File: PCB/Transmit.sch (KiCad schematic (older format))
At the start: 8 parts

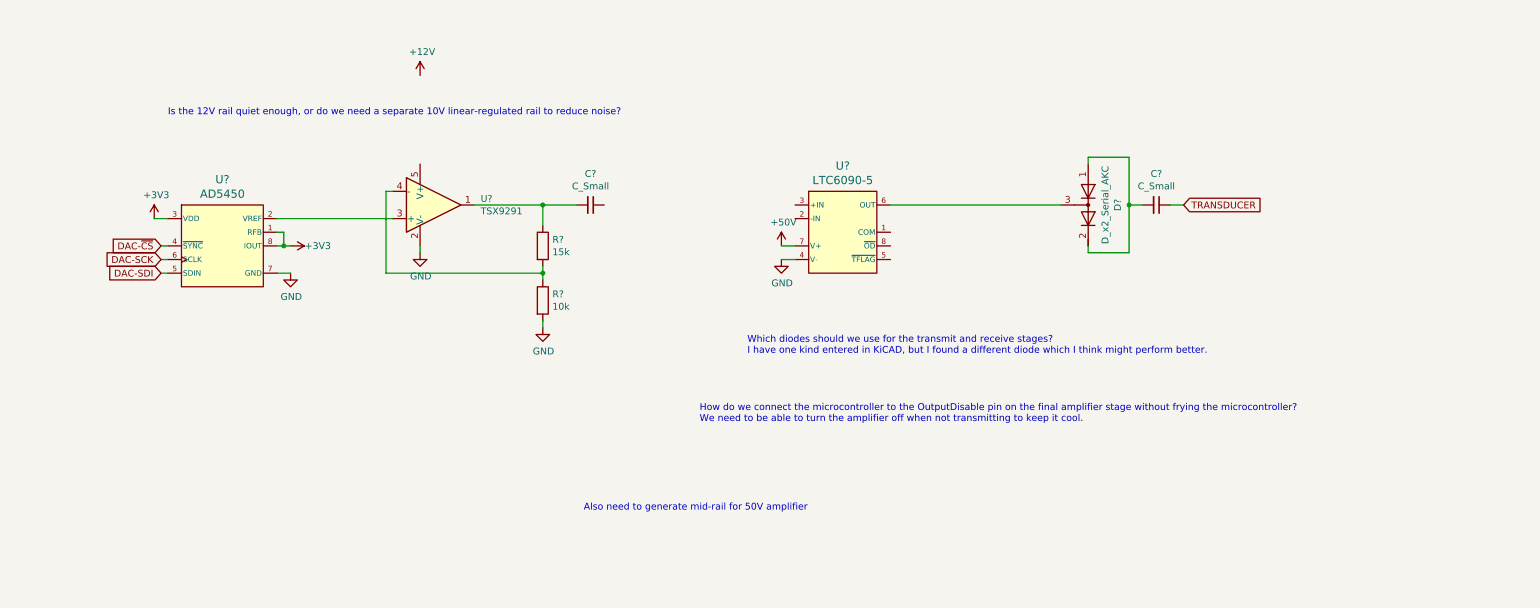
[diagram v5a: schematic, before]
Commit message: Switch to diodes that will waste less transmit power, add amplifier to generate transmit midrail, add enable signal to final amplifier
Enable signal to final amplifier is important, as it will allow us to conserve power when not transmitting. This should help keep the amplifier from overheating.
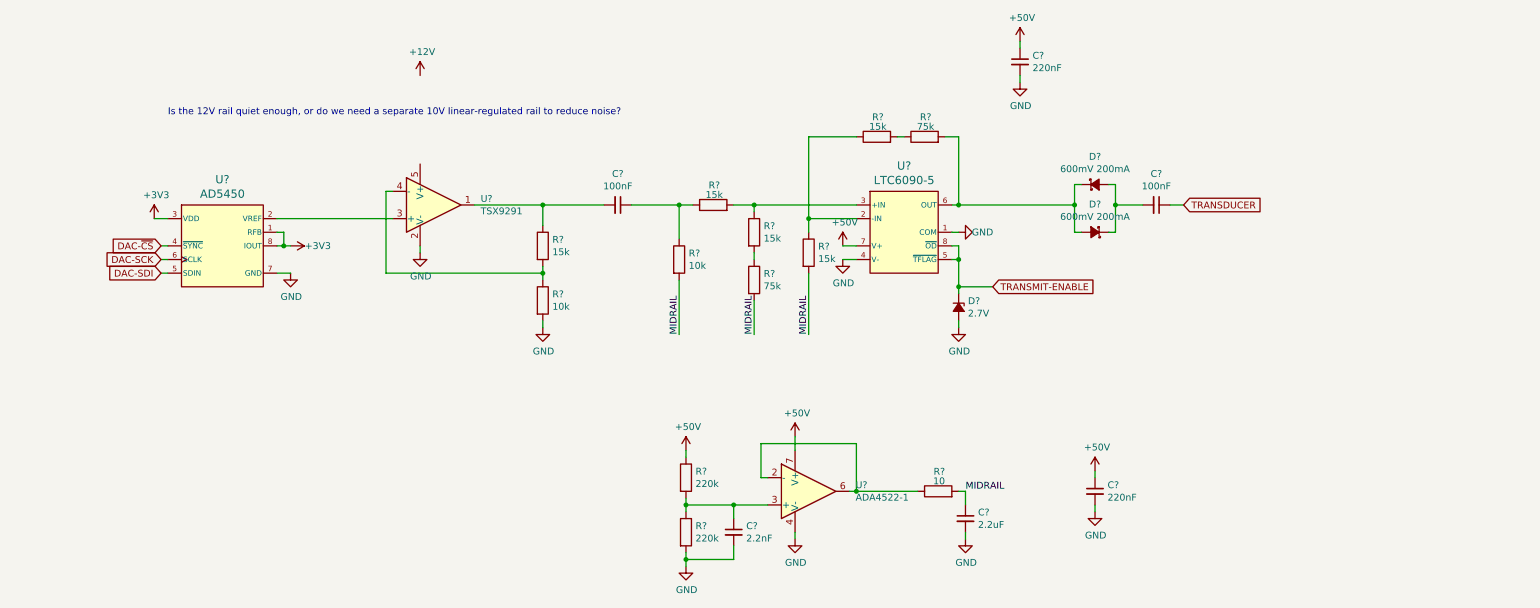
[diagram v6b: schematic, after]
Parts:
- removed C?: C_Small, symbol Device:C_Small
- removed D?: D_x2_Serial_AKC, Parts:MMBD7000L, symbol Device:D_x2_Serial_AKC
- added C?: 100nF, Capacitors_SMD:C_1206_HandSoldering, symbol Device:C_Small
- added C?: 2.2uF, Capacitors_SMD:C_1210_HandSoldering, symbol Device:C_Small
- added C? (x2): 220nF, Capacitors_SMD:C_1206_HandSoldering, symbol Device:C_Small
- added C?: 2.2nF, Capacitors_SMD:C_0603_HandSoldering, symbol Device:C_Small
- added D? (x2): 600mV 200mA, Diodes_SMD:D_SOD-523, symbol Device:D_Schottky_Small_ALT
- added D?: 2.7V, Diodes_SMD:D_SOD-123, symbol Device:D_Zener_Small_ALT
- added R? (x4): 15k, Resistors_SMD:R_0603_HandSoldering, symbol Device:R
- added R? (x2): 75k, Resistors_SMD:R_0603_HandSoldering, symbol Device:R
- added R?: 10, Resistors_SMD:R_0603_HandSoldering, symbol Device:R
- added R? (x2): 220k, Resistors_SMD:R_0603_HandSoldering, symbol Device:R
- added R?: 10k, Resistors_SMD:R_0603_HandSoldering, symbol Device:R
- added U?: ADA4522-1, Parts:SSOP8, symbol Parts:ADA4522-1
- C?: value C_Small -> 100nF; footprint (none) -> Capacitors_SMD:C_1206_HandSoldering
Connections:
- net +50V: now also C?.1, C?.1, R?.1, U?.7 (V+)
- net GND: now also U?.1 (COM), C?.2, C?.2, C?.2, C?.2, D?.2 (A), R?.2, U?.4 (V-)
- net TRANSDUCER: now also C?.1
- net at U?.6 (OUT): now also D?.1 (K), D?.2 (A), R?.2
- net at C?.1: now also R?.1, R?.1
- net at U?.2 (-IN): now also R?.1, R?.1
- net at U?.3 (+IN): now also R?.1, R?.2
- net TRANSMIT-ENABLE: now reaches U?.5 (~TFLAG)
- net TRANSMIT-ENABLE: now also U?.8 (~OD), D?.1 (K)
- new net: R?.1, R?.2 (x2)
- new net: C?.2, D?.1 (K), D?.2 (A)
- new net: R?.1, U?.2 (-), U?.6
- new net: C?.1, R?.1, R?.2, U?.3 (+)
- new net MIDRAIL: C?.1, R?.2, R?.2, R?.2, R?.2
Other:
- note removed: "Also need to generate mid-rail for 50V amplifier"
- note removed: "How do we connect the microcontroller to the OutputDisable pin on the final amplifier stage without frying the microcontroller?\nWe need to be able to turn the amplifier off when not transmitting to keep it cool."
- note removed: "Which diodes should we use for the transmit and receive stages?\nI have one kind entered in KiCAD, but I found a different diode which I think might perform better."
- moved on the sheet: C?, U?

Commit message: Add decoupling for other FPGA supplies
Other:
- note added: "Needs decoupling cap"
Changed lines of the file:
@@
 Wire Wire Line
 	8650 5800 8650 5850
+Text Notes 3250 3100 0    50   ~ 0
+Needs decoupling cap
 $EndSCHEMATC

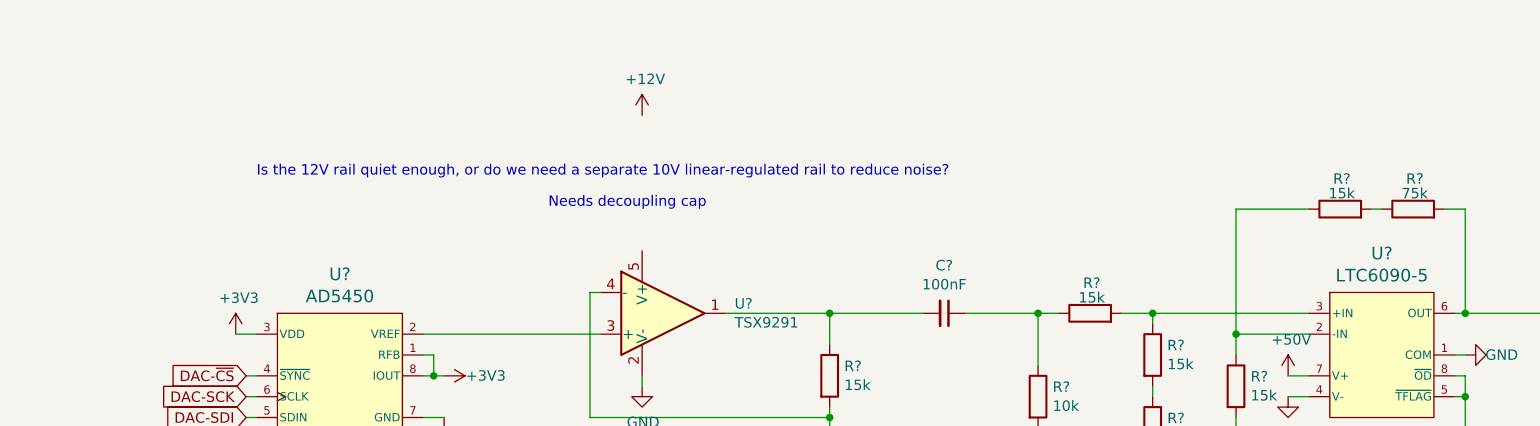
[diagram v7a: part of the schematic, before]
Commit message: Add decoupling capacitors for components without
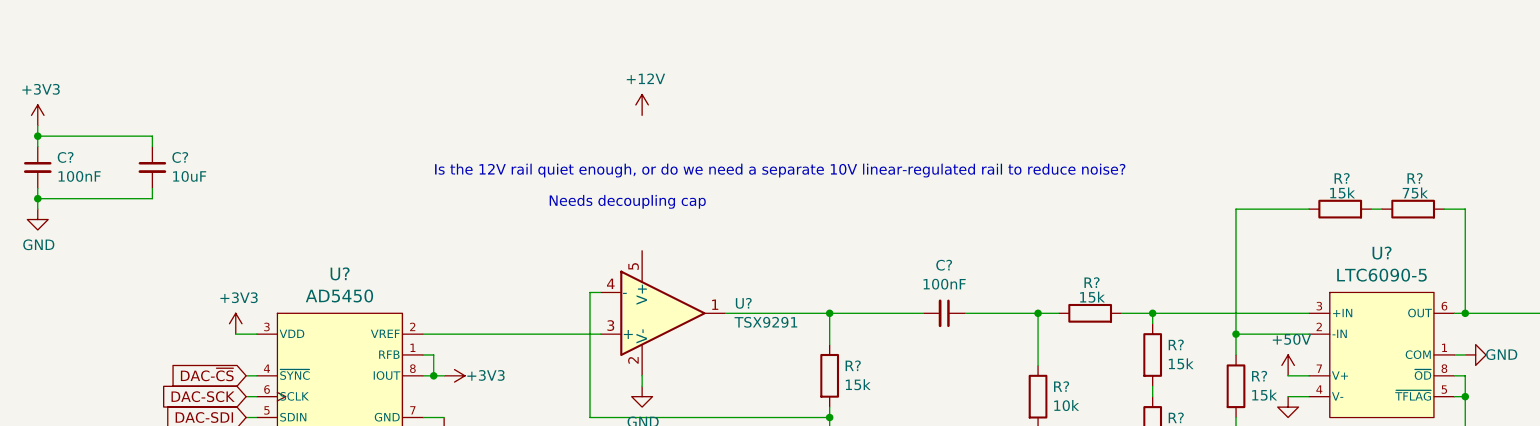
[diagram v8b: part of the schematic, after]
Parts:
- added C?: 100nF, Capacitors_SMD:C_0603_HandSoldering, symbol Device:C_Small
- added C?: 10uF, Capacitors_SMD:C_0805_HandSoldering, symbol Device:C_Small
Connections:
- net +3V3: now also C?.1, C?.1
- net GND: now also C?.2, C?.2
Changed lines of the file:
@@
 	1    0    0    -1
 $EndComp
-Text Notes 1850 2950 0    50   ~ 0
+Text Notes 2700 2950 0    50   ~ 0
 Is the 12V rail quiet enough, or do we need a separate 10V linear-regulated rail to reduce noise?
 $Comp
@@
 Text Notes 3250 3100 0    50   ~ 0
 Needs decoupling cap
+$Comp
+L power:GND #PWR?
+U 1 1 5E3B7B63
+P 800 3100
+F 0 "#PWR?" H 800 2850 50  0001 C CNN
+F 1 "GND" H 805 2927 50  0000 C CNN
+F 2 "" H 800 3100 50  0001 C CNN
+F 3 "" H 800 3100 50  0001 C CNN
+	1    800  3100
+	1    0    0    -1
+$EndComp
+$Comp
+L Device:C_Small C?
+U 1 1 5E3B80F6
+P 800 2900
+F 0 "C?" H 892 2946 50  0000 L CNN
+F 1 "100nF" H 892 2855 50  0000 L CNN
+F 2 "Capacitors_SMD:C_0603_HandSoldering" H 800 2900 50  0001 C CNN
+F 3 "https://www.digikey.ca/product-detail/en/w-rth-elektronik/885012206020/732-7939-1-ND/5454566" H 800 2900 50  0001 C CNN
+	1    800  2900
+	1    0    0    -1
+$EndComp
+$Comp
+L power:+3V3 #PWR?
+U 1 1 5E3B8767
+P 800 2700
+F 0 "#PWR?" H 800 2550 50  0001 C CNN
+F 1 "+3V3" H 815 2873 50  0000 C CNN
+F 2 "" H 800 2700 50  0001 C CNN
+F 3 "" H 800 2700 50  0001 C CNN
+	1    800  2700
+	1    0    0    -1
+$EndComp
+$Comp
+L Device:C_Small C?
+U 1 1 5E3BD08F
+P 1350 2900
+F 0 "C?" H 1442 2946 50  0000 L CNN
+F 1 "10uF" H 1442 2855 50  0000 L CNN
+F 2 "Capacitors_SMD:C_0805_HandSoldering" H 1350 2900 50  0001 C CNN
+F 3 "https://www.digikey.ca/product-detail/en/kemet/C0805C106K8PACTU/399-4925-1-ND/1090920" H 1350 2900 50  0001 C CNN
+	1    1350 2900
+	1    0    0    -1
+$EndComp
+Wire Wire Line
+	800  2700 800  2750
+Wire Wire Line
+	800  2750 1350 2750
+Wire Wire Line
+	1350 2750 1350 2800
+Connection ~ 800  2750
+Wire Wire Line
+	800  2750 800  2800
+Wire Wire Line
+	800  3000 800  3050
+Wire Wire Line
+	800  3050 1350 3050
+Wire Wire Line
+	1350 3050 1350 3000
+Connection ~ 800  3050
+Wire Wire Line
+	800  3050 800  3100
 $EndSCHEMATC
